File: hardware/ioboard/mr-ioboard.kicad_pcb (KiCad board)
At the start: 4 copper layers, 65 x 80 mm, 140 parts, among them J1 Conn_01x40_Shielded, J2 USB_C_Receptacle_USB2.0, J3 Conn_01x06, J4 Micro_SD_Card_Det, J5 Conn_01x04, J6 Conn_01x02, Q1 2N7002, SW1 SW_Push, SW2 SW_Push, SW3 SW_Push, SW4 SW_Push, SW5 SW_Push, U1 TPS62822, U10 F1C200S, U11 TPS54202DDC, U2 TPS56637, U3 TPD2E2U06, U4 DS90C363, U5 TPD2E2U06, U6 LD3985M28R_SOT23, U7 TPS62822, U8 FUSB302BMPX, U9 TPD2E2U06, Y1 24MHz

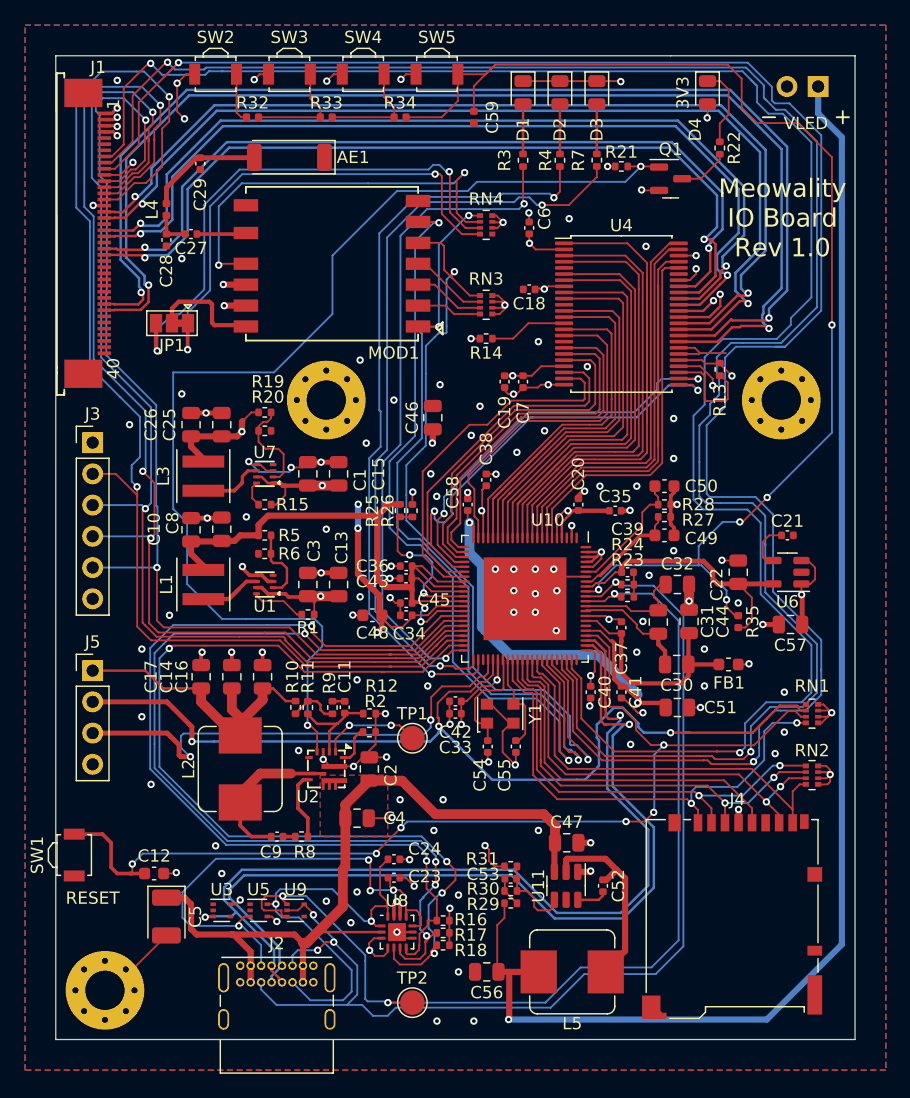
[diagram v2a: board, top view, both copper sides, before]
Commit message: Update IO board PCB layout with new regs
Signed-off-by: gatecat <gatecat@ds0.me>
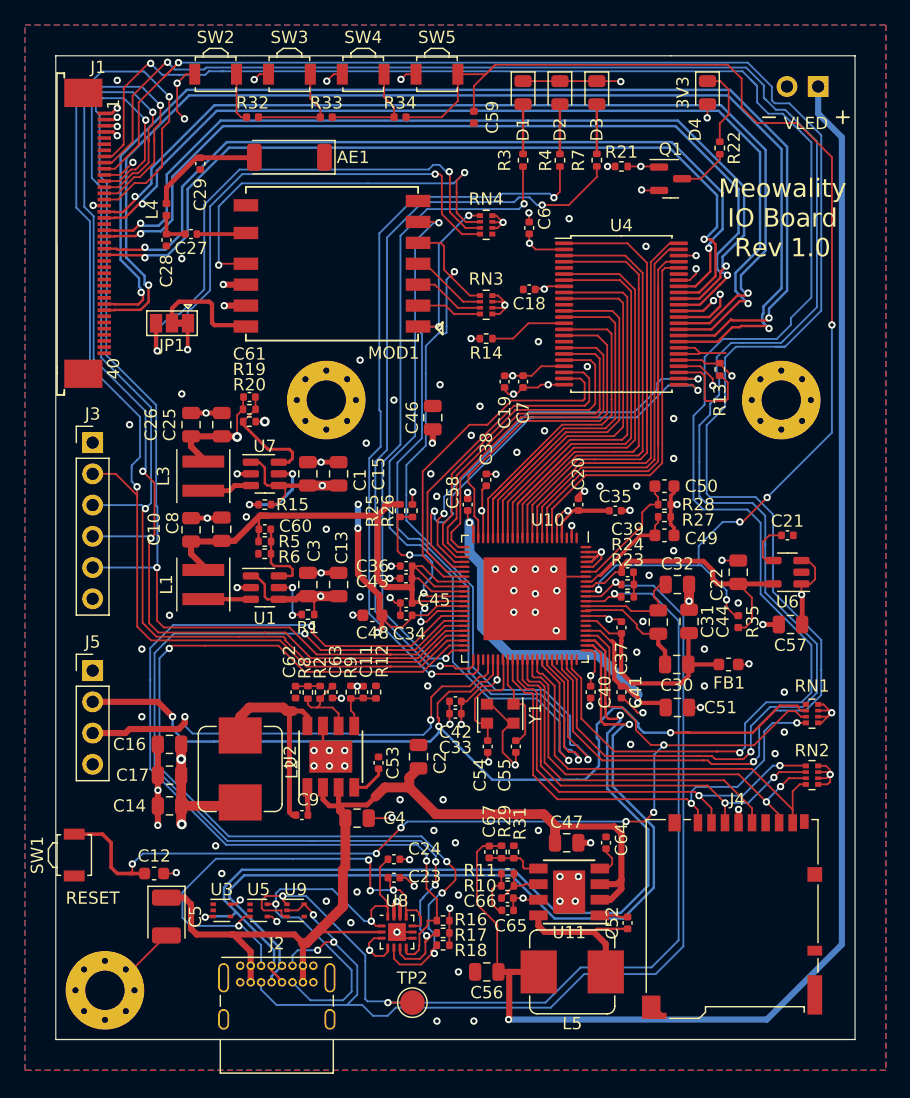
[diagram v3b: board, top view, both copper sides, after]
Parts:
- removed R30: 100k, Resistor_SMD:R_0402_1005Metric
- removed TP1: EN, TestPoint:TestPoint_Pad_D2.0mm
- added C60: 100p, Capacitor_SMD:C_0402_1005Metric, F.Cu at (117.0, 88.5)
- added C61: 100p, Capacitor_SMD:C_0402_1005Metric, F.Cu at (115.8, 77.8)
- added C62: 2.7n, Capacitor_SMD:C_0402_1005Metric, F.Cu at (119.5, 101.8)
- added C63: 33p, Capacitor_SMD:C_0402_1005Metric, F.Cu at (122.5, 101.8)
- added C64: 10n, Capacitor_SMD:C_0402_1005Metric, F.Cu at (144.8, 114.0)
- added C65: 2.7n, Capacitor_SMD:C_0402_1005Metric, F.Cu at (136.8, 119.5)
- added C66: 33p, Capacitor_SMD:C_0402_1005Metric, F.Cu at (136.7, 118.5)
- added C67: DNP, Capacitor_SMD:C_0402_1005Metric, F.Cu at (135.2, 114.8)
- C11: value 100p -> DNP
- C53: value 100p -> 10n
- L1, L3: value XFL4015-471MEB -> XFL4015-222MEC
- L2: value 2.2u -> 4.7u
- L5: value 15u -> 4.7u
- R10, R8: value 0 -> 31.6k
- R11: value 45.3k -> 31.6k
- R2: value NC -> 31.6k
- R29: value 49.9 -> 52.3k
- R31: value 13.3k -> 10k
- R9: value 20k -> 31.6k
- U1, U7: value TPS62822 -> AP3402; footprint meowality:TI_VSON-HR_1.5x2mm_p0.5mm -> Package_TO_SOT_SMD:TSOT-23-6
- U11: value TPS54202DDC -> AP64501; footprint Package_TO_SOT_SMD:SOT-23-6 -> Package_SO:Diodes_SO-8EP
- U2: value TPS56637 -> AP64501; footprint meowality:VQFN10-HR -> Package_SO:Diodes_SO-8EP
- moved R10 22.5 mm to (136.8, 117.5), turned to 180 degrees
- moved R11 21.1 mm to (136.8, 116.5), turned to 180 degrees
- moved C53 14.3 mm to (126.2, 107.5), turned to -90 degrees
- moved R8 11.7 mm to (120.5, 101.8), turned to 90 degrees
- moved C14 11.7 mm to (109.2, 111.0), turned to 180 degrees
- moved C16 9.36 mm to (109.2, 106.0), turned to 180 degrees
- moved C17 8.40 mm to (109.2, 108.5), turned to 180 degrees
- moved R2 5.14 mm to (121.5, 101.8), turned to 90 degrees
- moved R29 4.24 mm to (136.2, 114.8), turned to -90 degrees
- moved C2 4.12 mm to (129.5, 107.0)
- moved C52 3.62 mm to (146.5, 120.5), turned to -90 degrees
- moved C9 2.67 mm to (120.0, 111.8), turned to 0 degrees
- moved R9 1.95 mm to (124.0, 101.8)
- moved C11 1.94 mm to (125.0, 101.8)
- moved R12 1.83 mm to (126.0, 101.8), turned to 90 degrees
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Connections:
- C11 pad 1: Net-(C11-Pad1) -> +3V3
- C53 pad 1: Net-(C53-Pad1) -> GND
- L2 pad 1: Net-(C9-Pad2) -> Net-(C9-Pad1)
- R10 pad 1: +3V3 -> Net-(C66-Pad1)
- R10 pad 2: Net-(R10-Pad2) -> Net-(C65-Pad1)
- R11 pad 1: Net-(R10-Pad2) -> Net-(C66-Pad1)
- R11 pad 2: Net-(C11-Pad2) -> Net-(C65-Pad1)
- R19 pad 2: Net-(R19-Pad2) -> Net-(C61-Pad2)
- R2 pad 1: Net-(R2-Pad1) -> Net-(C63-Pad1)
- R2 pad 2: GND -> Net-(C62-Pad1)
- R20 pad 1: Net-(R19-Pad2) -> Net-(C61-Pad2)
- R29 pad 2: Net-(C53-Pad1) -> Net-(C67-Pad2)
- R31 pad 1: Net-(C53-Pad2) -> Net-(C67-Pad2)
- R5 pad 2: Net-(R5-Pad2) -> Net-(C60-Pad2)
- R6 pad 1: Net-(R5-Pad2) -> Net-(C60-Pad2)
- R8 pad 1: Net-(R8-Pad1) -> Net-(C63-Pad1)
- R8 pad 2: Net-(C9-Pad1) -> Net-(C62-Pad1)
- R9 pad 1: Net-(C11-Pad1) -> +3V3
- R9 pad 2: Net-(R10-Pad2) -> Net-(C11-Pad2)
- U1 pad 2: Net-(R5-Pad2) -> GND
- U1 pad 3: GND -> Net-(L1-Pad1)
- U1 pad 4: unconnected-(U1-Pad4) -> +3V3
- U1 pad 5: GND -> Net-(R1-Pad2)
- U1 pad 6: Net-(L1-Pad1) -> Net-(C60-Pad2)
- U11 pad 1: GND -> Net-(C52-Pad1)
- U11 pad 2: Net-(C52-Pad2) -> /VBUS
- U11 pad 4: Net-(C53-Pad2) -> Net-(C64-Pad2)
- U11 pad 5: unconnected-(U11-Pad5) -> Net-(C67-Pad2)
- U11 pad 6: Net-(C52-Pad1) -> Net-(C66-Pad1)
- U2 pad 1: Net-(TP1-Pad1) -> Net-(C9-Pad2)
- U2 pad 2: Net-(C11-Pad2) -> /VBUS
- U2 pad 3: GND -> /VBUS
- U2 pad 4: /3V3_PG -> Net-(C53-Pad2)
- U2 pad 5: unconnected-(U2-Pad5) -> Net-(C11-Pad2)
- U2 pad 6: Net-(C9-Pad2) -> Net-(C63-Pad1)
- U2 pad 7: Net-(R8-Pad1) -> GND
- U2 pad 8: /VBUS -> Net-(C9-Pad1)
- U7 pad 2: Net-(R19-Pad2) -> GND
- U7 pad 3: GND -> Net-(L3-Pad1)
- U7 pad 4: unconnected-(U7-Pad4) -> +3V3
- U7 pad 5: GND -> Net-(R15-Pad2)
- U7 pad 6: Net-(L3-Pad1) -> Net-(C61-Pad2)
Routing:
- net /3V3_PG: track 91.6 -> 2.61 mm, vias 2 -> 1
- net /VBUS: track 64.6 -> 85.0 mm
- net Net-(C9-Pad1): track 1.00 -> 18.9 mm
- net +3V3: track 137.8 -> 127.5 mm, vias 32 -> 35
- net Net-(C9-Pad2): track 12.3 -> 2.27 mm
- net Net-(C61-Pad2): track 0.00 -> 9.36 mm
- net Net-(TP1-Pad1): track 8.18 -> 0.00 mm, vias 2 -> 0
- net Net-(R19-Pad2): track 7.99 -> 0.00 mm
- net /VLED: track 113.2 -> 120.2 mm
- net Net-(C63-Pad1): track 0.00 -> 6.54 mm
- net Net-(C60-Pad2): track 0.00 -> 6.36 mm
- net Net-(R5-Pad2): track 6.08 -> 0.00 mm
- net GND: track 149.6 -> 143.9 mm, vias 127 -> 130
- net Net-(R8-Pad1): track 5.61 -> 0.00 mm
- net Net-(R15-Pad2): track 2.11 -> 7.12 mm, vias 0 -> 2
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- removed copper zone on F.Cu, net /VBUS

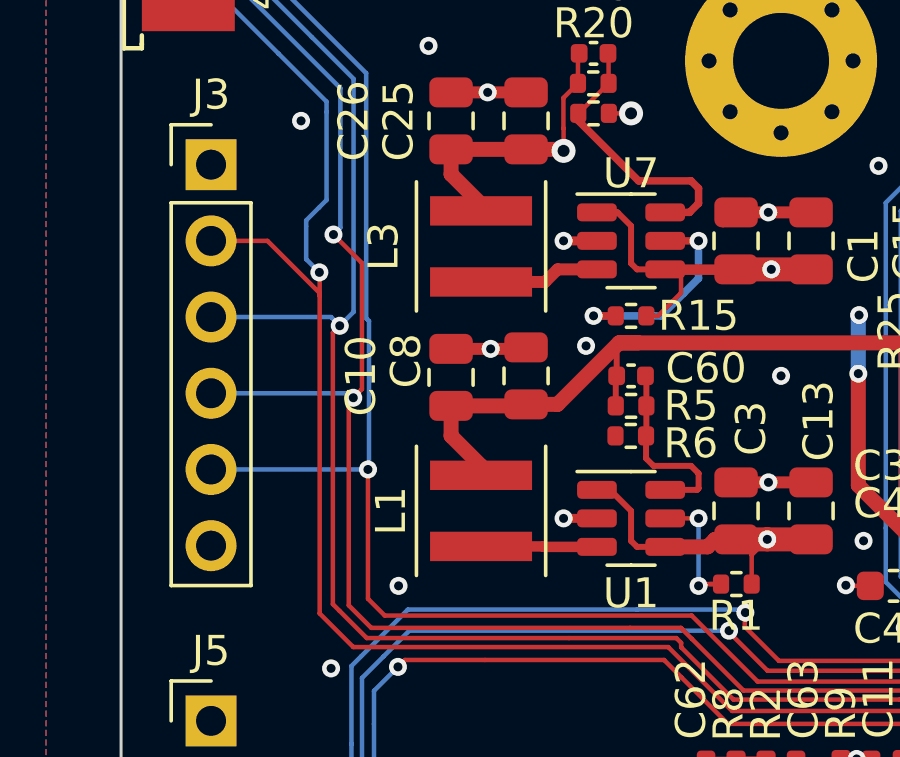
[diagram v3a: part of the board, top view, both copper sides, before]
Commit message: Update some inductor part numbers
Signed-off-by: gatecat <gatecat@ds0.me>
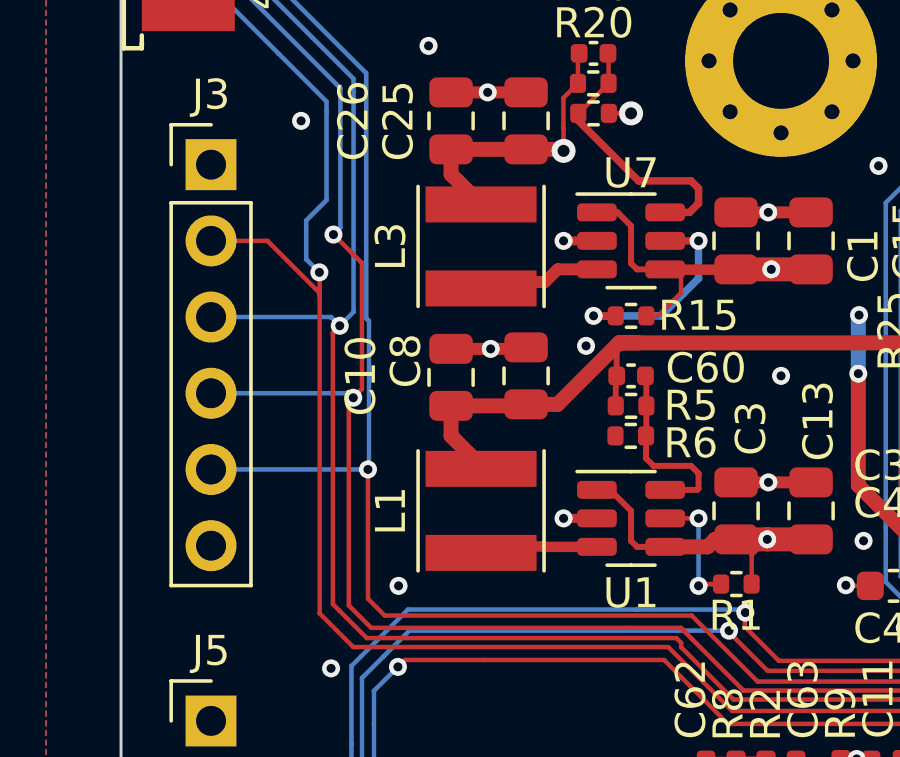
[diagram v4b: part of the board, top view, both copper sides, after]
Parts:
- L1, L3: value XFL4015-222MEC -> TYA40202R2M; footprint Inductor_SMD:L_Coilcraft_XxL4020 -> Inductor_SMD:L_Taiyo-Yuden_NR-40xx
- L2, L5: value 4.7u -> ASPI-7318-4R7M
